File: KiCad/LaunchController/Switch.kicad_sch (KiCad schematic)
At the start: 38 parts, among them J2 JMP_RUN, U5 U74HC14

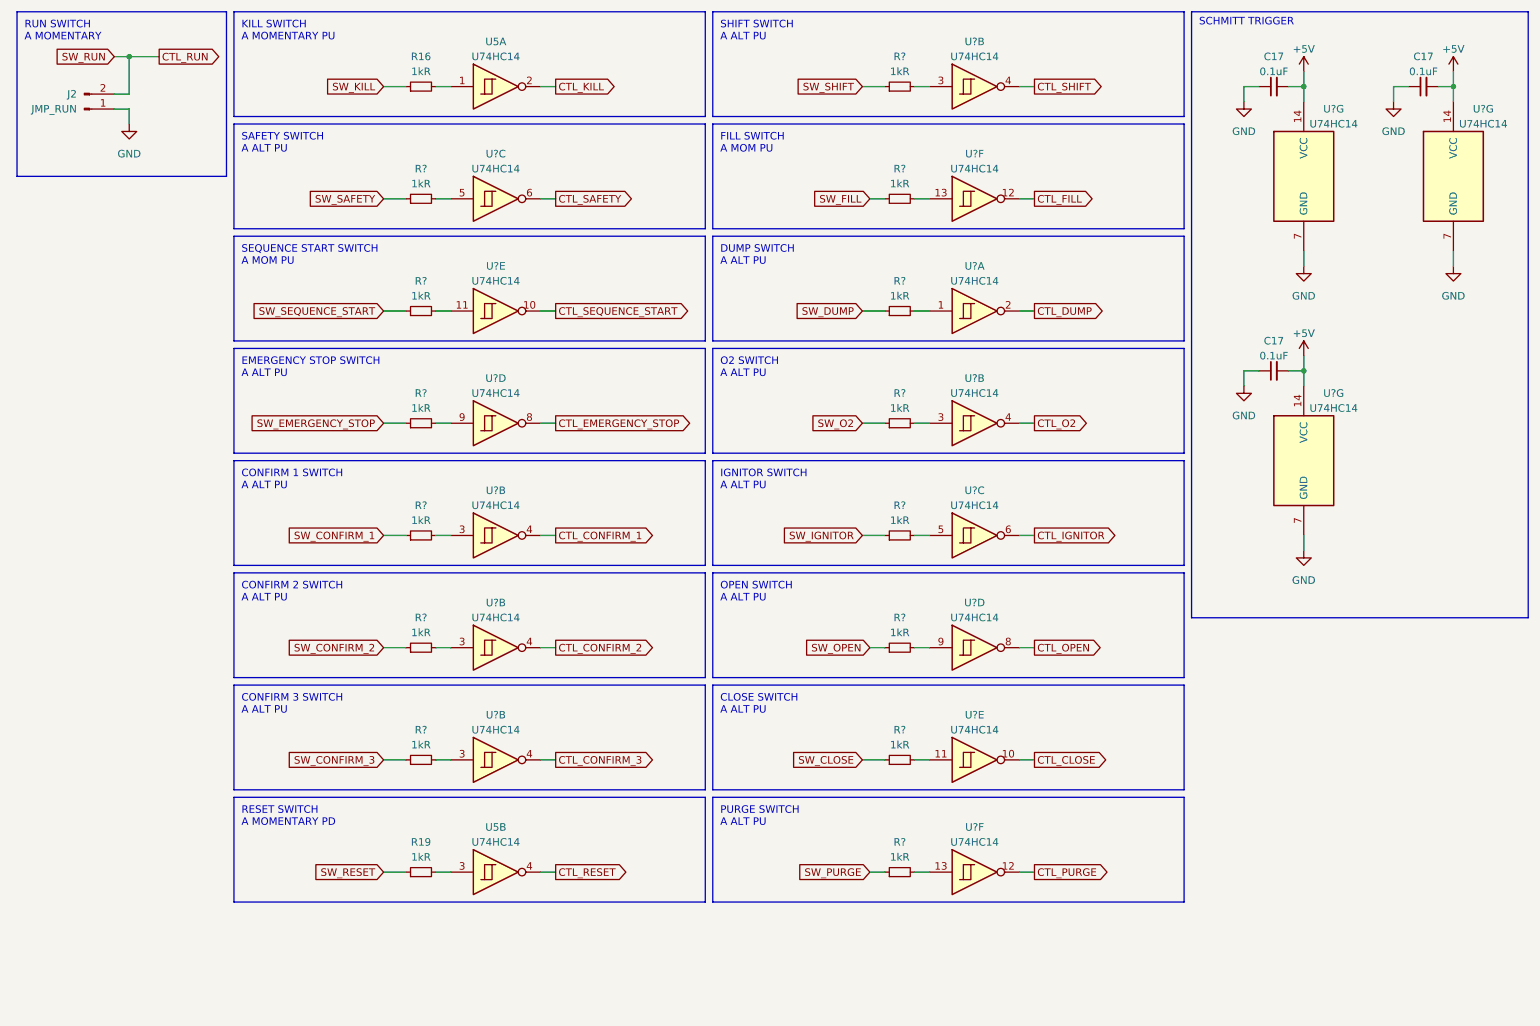
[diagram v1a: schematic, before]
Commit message: ランスイッチにチャタリング対策を追加
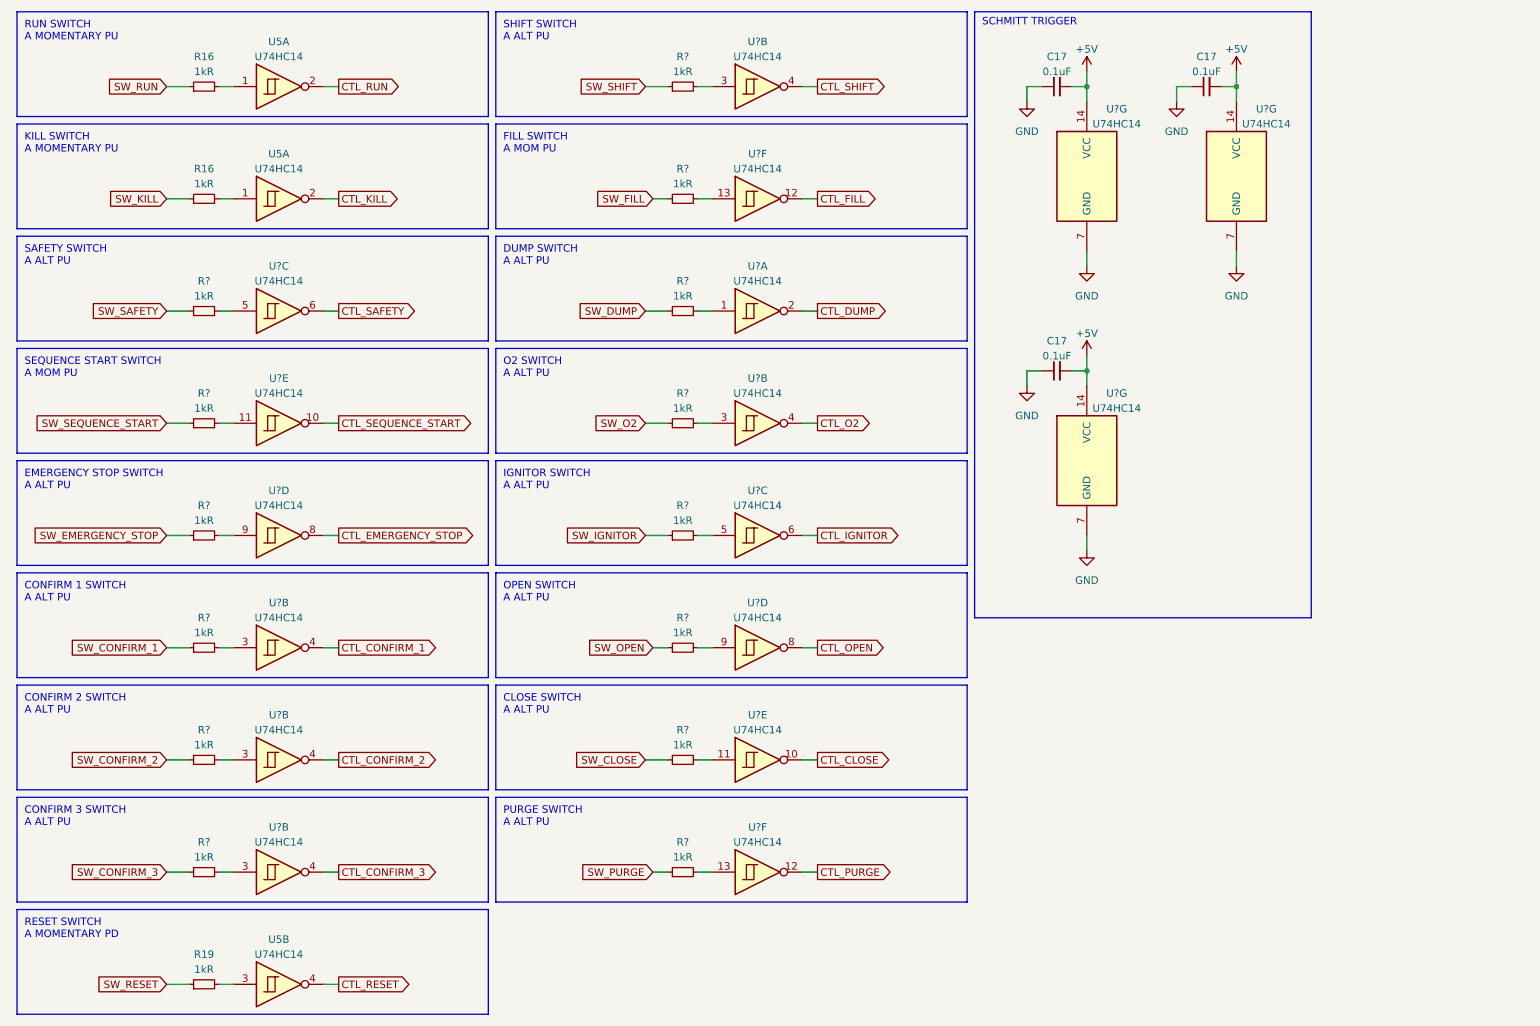
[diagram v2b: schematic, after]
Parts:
- removed J2: JMP_RUN, Connector_PinHeader_2.54mm:PinHeader_1x02_P2.54mm_Vertical, symbol Connector:Conn_01x02_Pin
- added R16: 1kR, Resistor_SMD:R_0603_1608Metric_Pad0.98x0.95mm_HandSolder, symbol Device:R_Small
- added U5: U74HC14, Package_DIP:DIP-14_W7.62mm, symbol 74xx:74HC14
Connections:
- net CTL_RUN: now also U5.2
- new net: R16.2, U5.1
- new net SW_RUN: R16.1
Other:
- note added: "RUN SWITCH A MOMENTARY PU"
- note removed: "RUN SWITCH A MOMENTARY"
- moved on the sheet: C17, R16, R19, R?, U5A, U5B, U?A, U?B, U?C, U?D, U?E, U?F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

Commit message: 配線終わらん
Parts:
- removed C17 (x3): 0.1uF, Capacitor_SMD:C_0603_1608Metric_Pad1.08x0.95mm_HandSolder, symbol Device:C_Small
- removed R16 (x2), R19, R? (x14): 1kR, Resistor_SMD:R_0603_1608Metric_Pad0.98x0.95mm_HandSolder, symbol Device:R_Small
- removed U5 (x2), U? (x17): U74HC14, Package_DIP:DIP-14_W7.62mm, symbol 74xx:74HC14
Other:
- note removed: "CLOSE SWITCH A ALT PU"
- note removed: "CONFIRM 1 SWITCH A ALT PU"
- note removed: "CONFIRM 2 SWITCH A ALT PU"
- note removed: "CONFIRM 3 SWITCH A ALT PU"
- note removed: "DUMP SWITCH A ALT PU"
- note removed: "EMERGENCY STOP SWITCH A ALT PU"
- note removed: "FILL SWITCH A MOM PU"
- note removed: "IGNITOR SWITCH A ALT PU"
- note removed: "KILL SWITCH A MOMENTARY PU"
- note removed: "O2 SWITCH A ALT PU"
- note removed: "OPEN SWITCH A ALT PU"
- note removed: "PURGE SWITCH A ALT PU"
- note removed: "RESET SWITCH A MOMENTARY PD"
- note removed: "RUN SWITCH A MOMENTARY PU"
- note removed: "SAFETY SWITCH A ALT PU"
- note removed: "SCHMITT TRIGGER"
- note removed: "SEQUENCE START SWITCH A MOM PU"
- note removed: "SHIFT SWITCH A ALT PU"

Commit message: シュミットトリガー無しで部品を配置
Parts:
- added C17 (x3): 0.1uF, Capacitor_SMD:C_0603_1608Metric_Pad1.08x0.95mm_HandSolder, symbol Device:C_Small
- added R16 (x2), R19, R? (x14): 1kR, Resistor_SMD:R_0603_1608Metric_Pad0.98x0.95mm_HandSolder, symbol Device:R_Small
- added U5, U? (x17): U74HC14, Package_DIP:DIP-14_W7.62mm, symbol 74xx:74HC14
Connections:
- new net: R?.2, U?.13 (x2)
- new net: R16.2, U5.1 (x2)
- new net: R?.2, U?.1
- new net: R?.2, U?.3 (x5)
- new net: R?.2, U?.9 (x2)
- new net: R?.2, U?.11 (x2)
- new net: R?.2, U?.5 (x2)
- new net: R19.2, U5.3
- new net +5V: C17.2, C17.2, C17.2, U?.14 (VCC), U?.14 (VCC), U?.14 (VCC)
- new net CTL_CLOSE: U?.10
- new net CTL_CONFIRM_1: U?.4
- new net CTL_CONFIRM_2: U?.4
- new net CTL_CONFIRM_3: U?.4
- new net CTL_DUMP: U?.2
- new net CTL_EMERGENCY_STOP: U?.8
- new net CTL_FILL: U?.12
- new net CTL_IGNITOR: U?.6
- new net CTL_KILL: U5.2
- new net CTL_O2: U?.4
- new net CTL_OPEN: U?.8
- new net CTL_PURGE: U?.12
- new net CTL_RESET: U5.4
- new net CTL_RUN: U5.2
- new net CTL_SAFETY: U?.6
- new net CTL_SEQUENCE_START: U?.10
- new net CTL_SHIFT: U?.4
- new net GND: C17.1, C17.1, C17.1, U?.7 (GND), U?.7 (GND), U?.7 (GND)
- new net SW_CLOSE: R?.1
- new net SW_CONFIRM_1: R?.1
- new net SW_CONFIRM_2: R?.1
- new net SW_CONFIRM_3: R?.1
- new net SW_DUMP: R?.1
- new net SW_EMERGENCY_STOP: R?.1
- new net SW_FILL: R?.1
- new net SW_IGNITOR: R?.1
- new net SW_KILL: R16.1
- new net SW_O2: R?.1
- new net SW_OPEN: R?.1
- new net SW_PURGE: R?.1
- new net SW_RESET: R19.1
- new net SW_RUN: R16.1
- new net SW_SAFETY: R?.1
- new net SW_SEQUENCE_START: R?.1
- new net SW_SHIFT: R?.1
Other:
- note added: "CLOSE SWITCH A ALT PU"
- note added: "CONFIRM 1 SWITCH A ALT PU"
- note added: "CONFIRM 2 SWITCH A ALT PU"
- note added: "CONFIRM 3 SWITCH A ALT PU"
- note added: "DUMP SWITCH A ALT PU"
- note added: "EMERGENCY STOP SWITCH A ALT PU"
- note added: "FILL SWITCH A MOM PU"
- note added: "IGNITOR SWITCH A ALT PU"
- note added: "KILL SWITCH A MOMENTARY PU"
- note added: "O2 SWITCH A ALT PU"
- note added: "OPEN SWITCH A ALT PU"
- note added: "PURGE SWITCH A ALT PU"
- note added: "RESET SWITCH A MOMENTARY PD"
- note added: "RUN SWITCH A MOMENTARY PU"
- note added: "SAFETY SWITCH A ALT PU"
- note added: "SCHMITT TRIGGER"
- note added: "SEQUENCE START SWITCH A MOM PU"
- note added: "SHIFT SWITCH A ALT PU"

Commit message: リセット
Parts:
- added R?: 1kR, Resistor_SMD:R_0603_1608Metric_Pad0.98x0.95mm_HandSolder, symbol Device:R_Small
- added U?: U74HC14, Package_DIP:DIP-14_W7.62mm, symbol 74xx:74HC14
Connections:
- net GND: now also R?.1
- new net: R?.2, U?.13
- no-connect marks 0 -> 1

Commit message: あとはDRC解決とビア打ち
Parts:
- U5, U? (x18): footprint Package_DIP:DIP-14_W7.62mm -> Package_SO:TSSOP-14_4.4x5mm_P0.65mm
